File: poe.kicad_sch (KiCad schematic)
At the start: 59 parts, among them IC1 TPS2378DDA, J1 B2B-XH-A_LF__SN_, J6 SS-74800-144, U3 TPS2373-3RGW, U4 URB4805YMD-30WR3

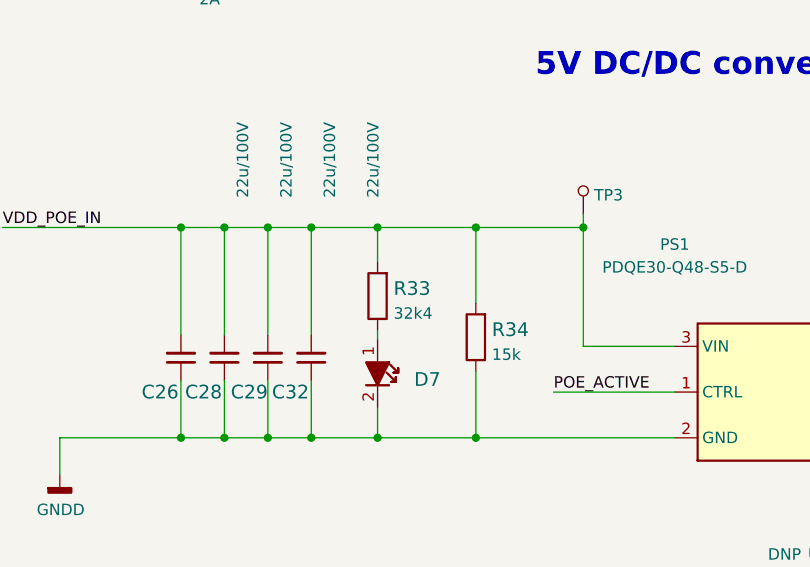
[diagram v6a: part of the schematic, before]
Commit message: Update R33 symbol and footprint
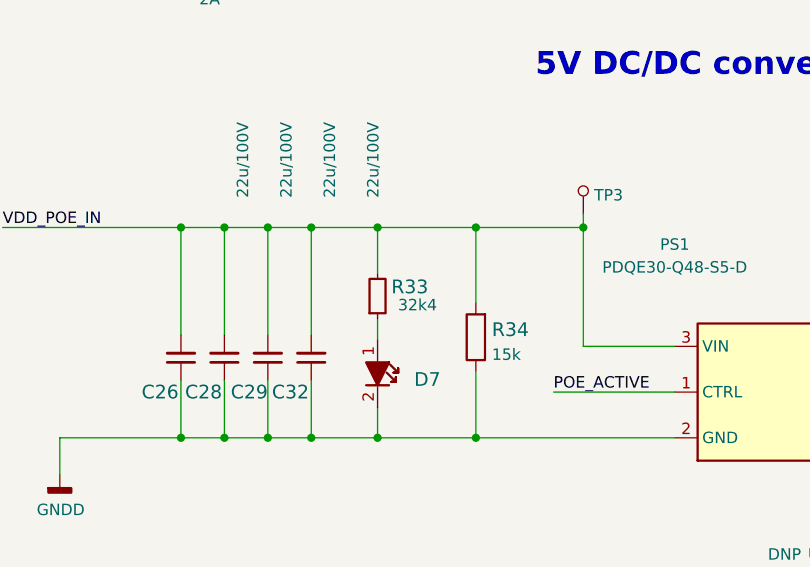
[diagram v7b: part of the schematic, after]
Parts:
- R33: footprint scalenode-cm4-baseboard-footprints:0805-res -> antmicro-footprints:R_0805_2012Metric; symbol scalenode-cm4-baseboard:R_32k4_0805 -> antmicroResistorsmisc:R_32k4_0805; Author (none) -> Antmicro; License (none) -> Apache-2.0; MPN ERA-6AEB3242V -> CR0805-FX-3242ELF; Manufacturer Panasonic -> Bourns; Tolerance (none) -> 1%
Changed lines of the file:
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@@
     (stroke (width 0) (type default) (color 0 0 0 0))
   )
-  (wire (pts (xy 243.586 188.468) (xy 243.586 189.484))
+  (wire (pts (xy 243.586 187.198) (xy 243.586 189.484))
     (stroke (width 0) (type default) (color 0 0 0 0))
   )
@@
     (stroke (width 0) (type default) (color 0 0 0 0))
   )
-  (wire (pts (xy 243.586 177.038) (xy 243.586 180.848))
+  (wire (pts (xy 243.586 177.038) (xy 243.586 182.118))
     (stroke (width 0) (type default) (color 0 0 0 0))
   )
@@
     (pin "2")
   )
-  (symbol (lib_id "scalenode-cm4-baseboard:R_32k4_0805") (at 243.586 184.658 90) (unit 1)
-    (in_bom yes) (on_board yes) (fields_autoplaced)
-    (property "Reference" "R33" (id 0) (at 245.364 183.8234 90)
+  (symbol (lib_id "antmicroResistorsmisc:R_32k4_0805") (at 243.586 187.198 90) (unit 1)
+    (in_bom yes) (on_board yes)
+    (property "Reference" "R33" (id 0) (at 245.11 183.642 90)
       (effects (font (size 1.524 1.524)) (justify right))
     )
-    (property "Value" "R_32k4_0805" (id 1) (at 247.396 184.658 0)
+    (property "Value" "R_32k4_0805" (id 1) (at 247.396 187.198 0)
       (effects (font (size 1.524 1.524)) hide)
     )
-    (property "Footprint" "scalenode-cm4-baseboard-footprints:0805-res" (id 2) (at 238.506 179.578 0)
-      (effects (font (size 1.524 1.524)) (justify left) hide)
+    (property "Footprint" "antmicro-footprints:R_0805_2012Metric" (id 2) (at 258.826 166.878 0)
+      (effects (font (size 1.27 1.27) (thickness 0.15)) (justify left bottom) hide)
     )
-    (property "Datasheet" "" (id 3) (at 243.586 184.658 0)
-      (effects (font (size 1.27 1.27)) hide)
+    (property "Datasheet" "https://www.bourns.com/docs/product-datasheets/cr.pdf" (id 3) (at 261.366 166.878 0)
+      (effects (font (size 1.27 1.27) (thickness 0.15)) (justify left bottom) hide)
     )
-    (property "Manufacturer" "Panasonic" (id 4) (at 233.426 179.578 0)
-      (effects (font (size 1.524 1.524)) (justify left) hide)
+    (property "Manufacturer" "Bourns" (id 4) (at 266.446 166.878 0)
+      (effects (font (size 1.27 1.27) (thickness 0.15)) (justify left bottom) hide)
     )
-    (property "MPN" "ERA-6AEB3242V" (id 5) (at 235.966 179.578 0)
-      (effects (font (size 1.524 1.524)) (justify left) hide)
+    (property "MPN" "CR0805-FX-3242ELF" (id 5) (at 263.906 166.878 0)
+      (effects (font (size 1.27 1.27) (thickness 0.15)) (justify left bottom) hide)
     )
-    (property "Val" "32k4" (id 6) (at 245.364 186.5885 90)
-      (effects (font (size 1.27 1.27)) (justify right))
+    (property "Val" "32k4" (id 6) (at 250.19 184.912 90)
+      (effects (font (size 1.27 1.27) (thickness 0.15)) (justify left bottom))
+    )
+    (property "License" "Apache-2.0" (id 7) (at 268.986 166.878 0)
+      (effects (font (size 1.27 1.27) (thickness 0.15)) (justify left bottom) hide)
+    )
+    (property "Author" "Antmicro" (id 8) (at 271.526 166.878 0)
+      (effects (font (size 1.27 1.27) (thickness 0.15)) (justify left bottom) hide)
+    )
+    (property "Tolerance" "1%" (id 9) (at 253.746 166.878 0)
+      (effects (font (size 1.27 1.27)) (justify left bottom) hide)
     )
     (pin "1")

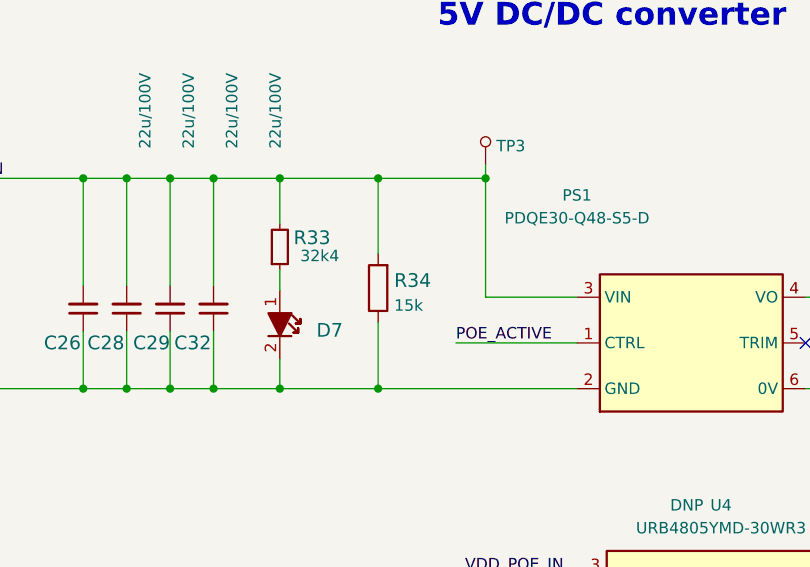
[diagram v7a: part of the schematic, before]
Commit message: Update R34 symbol and footprint
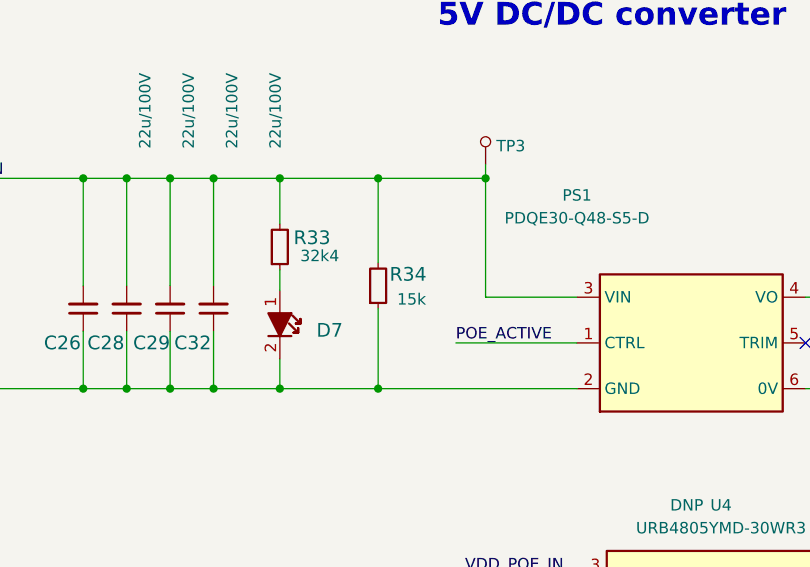
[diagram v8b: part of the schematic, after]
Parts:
- R34: footprint scalenode-cm4-baseboard-footprints:0603-res -> antmicro-footprints:R_0603_1608Metric; symbol scalenode-cm4-baseboard:R_15k_0603 -> antmicroResistors0603:R_15k_0603; Author (none) -> Antmicro; License (none) -> Apache-2.0; Manufacturer BOURNS -> Bourns; Tolerance (none) -> 1%
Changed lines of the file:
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@@
     (stroke (width 0) (type default) (color 0 0 0 0))
   )
-  (wire (pts (xy 254.508 193.04) (xy 254.508 200.406))
+  (wire (pts (xy 254.508 191.516) (xy 254.508 200.406))
     (stroke (width 0) (type default) (color 0 0 0 0))
   )
@@
     (stroke (width 0) (type default) (color 0 0 0 0))
   )
-  (wire (pts (xy 254.508 177.038) (xy 254.508 185.42))
+  (wire (pts (xy 254.508 177.038) (xy 254.508 186.436))
     (stroke (width 0) (type default) (color 0 0 0 0))
   )
@@
     (pin "1")
   )
-  (symbol (lib_id "scalenode-cm4-baseboard:R_15k_0603") (at 254.508 189.23 90) (unit 1)
-    (in_bom yes) (on_board yes) (fields_autoplaced)
-    (property "Reference" "R34" (id 0) (at 256.286 188.3954 90)
+  (symbol (lib_id "antmicroResistors0603:R_15k_0603") (at 254.508 191.516 90) (unit 1)
+    (in_bom yes) (on_board yes)
+    (property "Reference" "R34" (id 0) (at 255.778 187.706 90)
       (effects (font (size 1.524 1.524)) (justify right))
     )
-    (property "Value" "R_15k_0603" (id 1) (at 258.318 189.23 0)
+    (property "Value" "R_15k_0603" (id 1) (at 258.318 191.516 0)
       (effects (font (size 1.524 1.524)) hide)
     )
-    (property "Footprint" "scalenode-cm4-baseboard-footprints:0603-res" (id 2) (at 249.428 184.15 0)
-      (effects (font (size 1.524 1.524)) (justify left) hide)
+    (property "Footprint" "antmicro-footprints:R_0603_1608Metric" (id 2) (at 269.748 171.196 0)
+      (effects (font (size 1.27 1.27) (thickness 0.15)) (justify left bottom) hide)
     )
-    (property "Datasheet" "" (id 3) (at 254.508 189.23 0)
-      (effects (font (size 1.27 1.27)) hide)
+    (property "Datasheet" "https://www.bourns.com/docs/product-datasheets/cr.pdf" (id 3) (at 272.288 171.196 0)
+      (effects (font (size 1.27 1.27) (thickness 0.15)) (justify left bottom) hide)
     )
-    (property "Manufacturer" "BOURNS" (id 4) (at 244.348 184.15 0)
-      (effects (font (size 1.524 1.524)) (justify left) hide)
+    (property "Manufacturer" "Bourns" (id 4) (at 277.368 171.196 0)
+      (effects (font (size 1.27 1.27) (thickness 0.15)) (justify left bottom) hide)
     )
-    (property "MPN" "CR0603-FX-1502ELF" (id 5) (at 246.888 184.15 0)
-      (effects (font (size 1.524 1.524)) (justify left) hide)
+    (property "MPN" "CR0603-FX-1502ELF" (id 5) (at 274.828 171.196 0)
+      (effects (font (size 1.27 1.27) (thickness 0.15)) (justify left bottom) hide)
     )
-    (property "Val" "15k" (id 6) (at 256.286 191.1605 90)
-      (effects (font (size 1.27 1.27)) (justify right))
+    (property "Val" "15k" (id 6) (at 259.842 189.738 90)
+      (effects (font (size 1.27 1.27) (thickness 0.15)) (justify left bottom))
+    )
+    (property "License" "Apache-2.0" (id 7) (at 279.908 171.196 0)
+      (effects (font (size 1.27 1.27) (thickness 0.15)) (justify left bottom) hide)
+    )
+    (property "Author" "Antmicro" (id 8) (at 282.448 171.196 0)
+      (effects (font (size 1.27 1.27) (thickness 0.15)) (justify left bottom) hide)
+    )
+    (property "Tolerance" "1%" (id 9) (at 264.668 171.196 0)
+      (effects (font (size 1.27 1.27)) (justify left bottom) hide)
     )
     (pin "1")
